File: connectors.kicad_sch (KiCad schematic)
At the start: 31 parts, among them J2 SM08B-SRSS-TB, U23 SDA, U26 SCL, U31 9V

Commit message: routing...
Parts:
- removed TP4: M1, TestPoint:TestPoint_Pad_D1.0mm, symbol Connector:TestPoint
- removed TP5: M2, TestPoint:TestPoint_Pad_D1.0mm, symbol Connector:TestPoint
- removed TP6: M3, TestPoint:TestPoint_Pad_D1.0mm, symbol Connector:TestPoint
- removed TP7: M4, TestPoint:TestPoint_Pad_D1.0mm, symbol Connector:TestPoint
- added TP10: 5V_USB, TestPoint:TestPoint_Pad_D1.0mm, symbol Connector:TestPoint
- added TP11: VCC_ICM, TestPoint:TestPoint_Pad_D1.0mm, symbol Connector:TestPoint
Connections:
- new net 5V_USB: TP10.1
- new net VCC_ICM: TP11.1

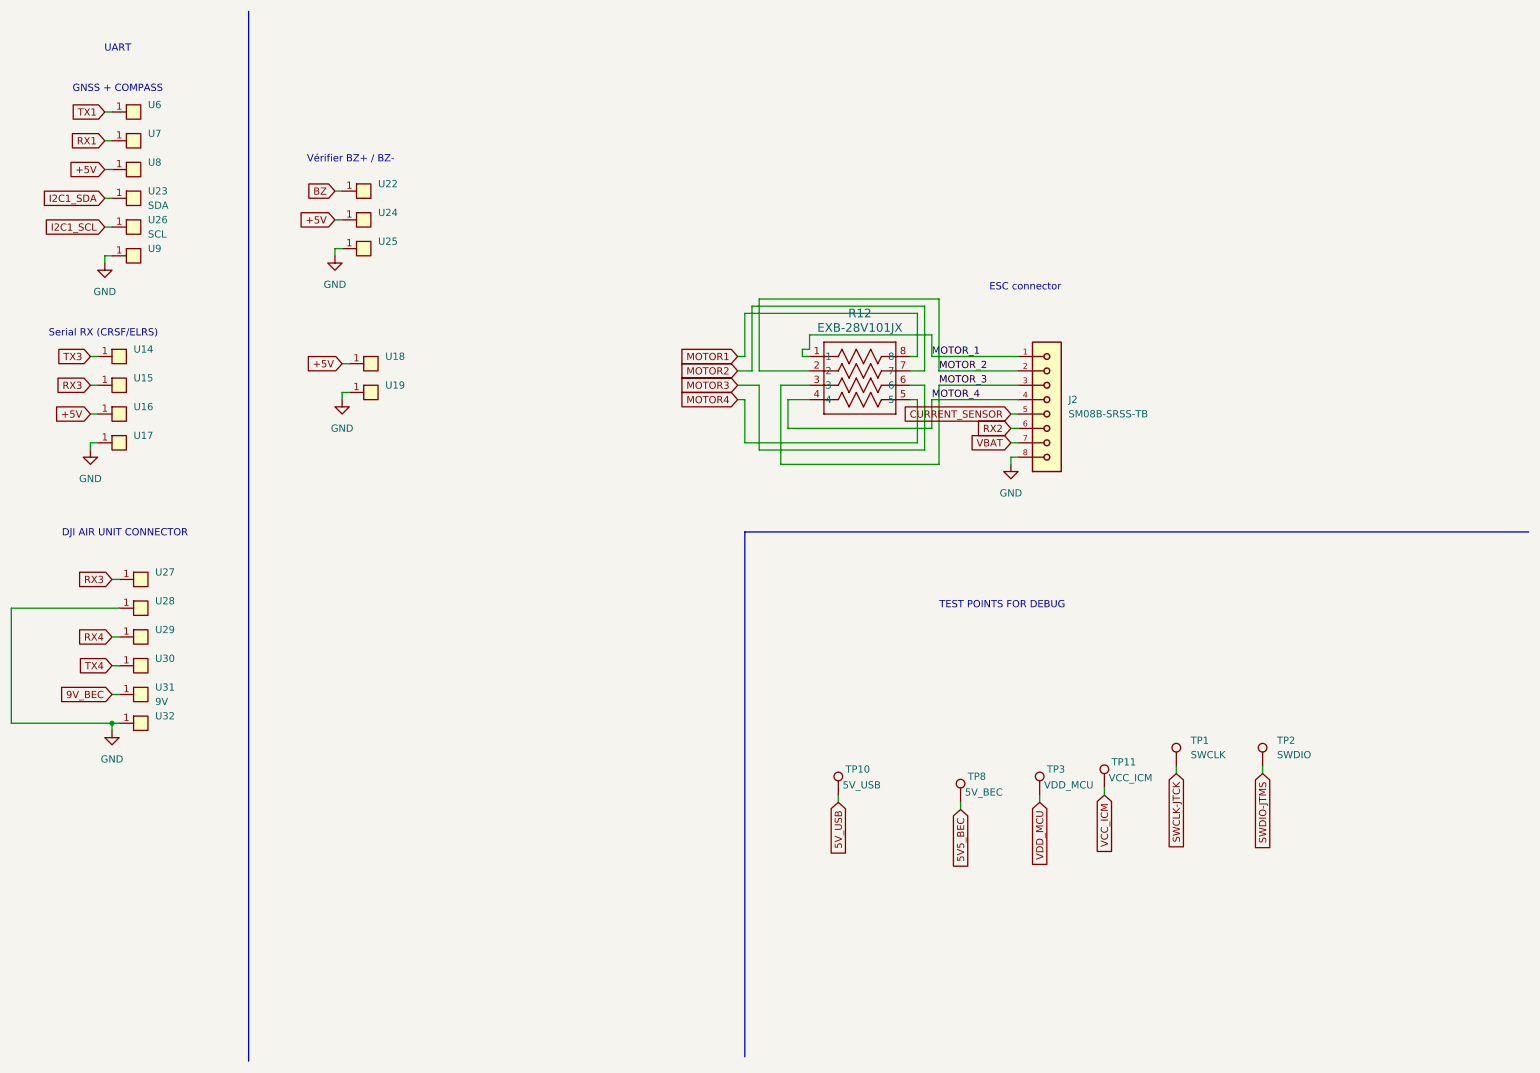
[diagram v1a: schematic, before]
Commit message: changed barometer to BMP580 and completed BOM
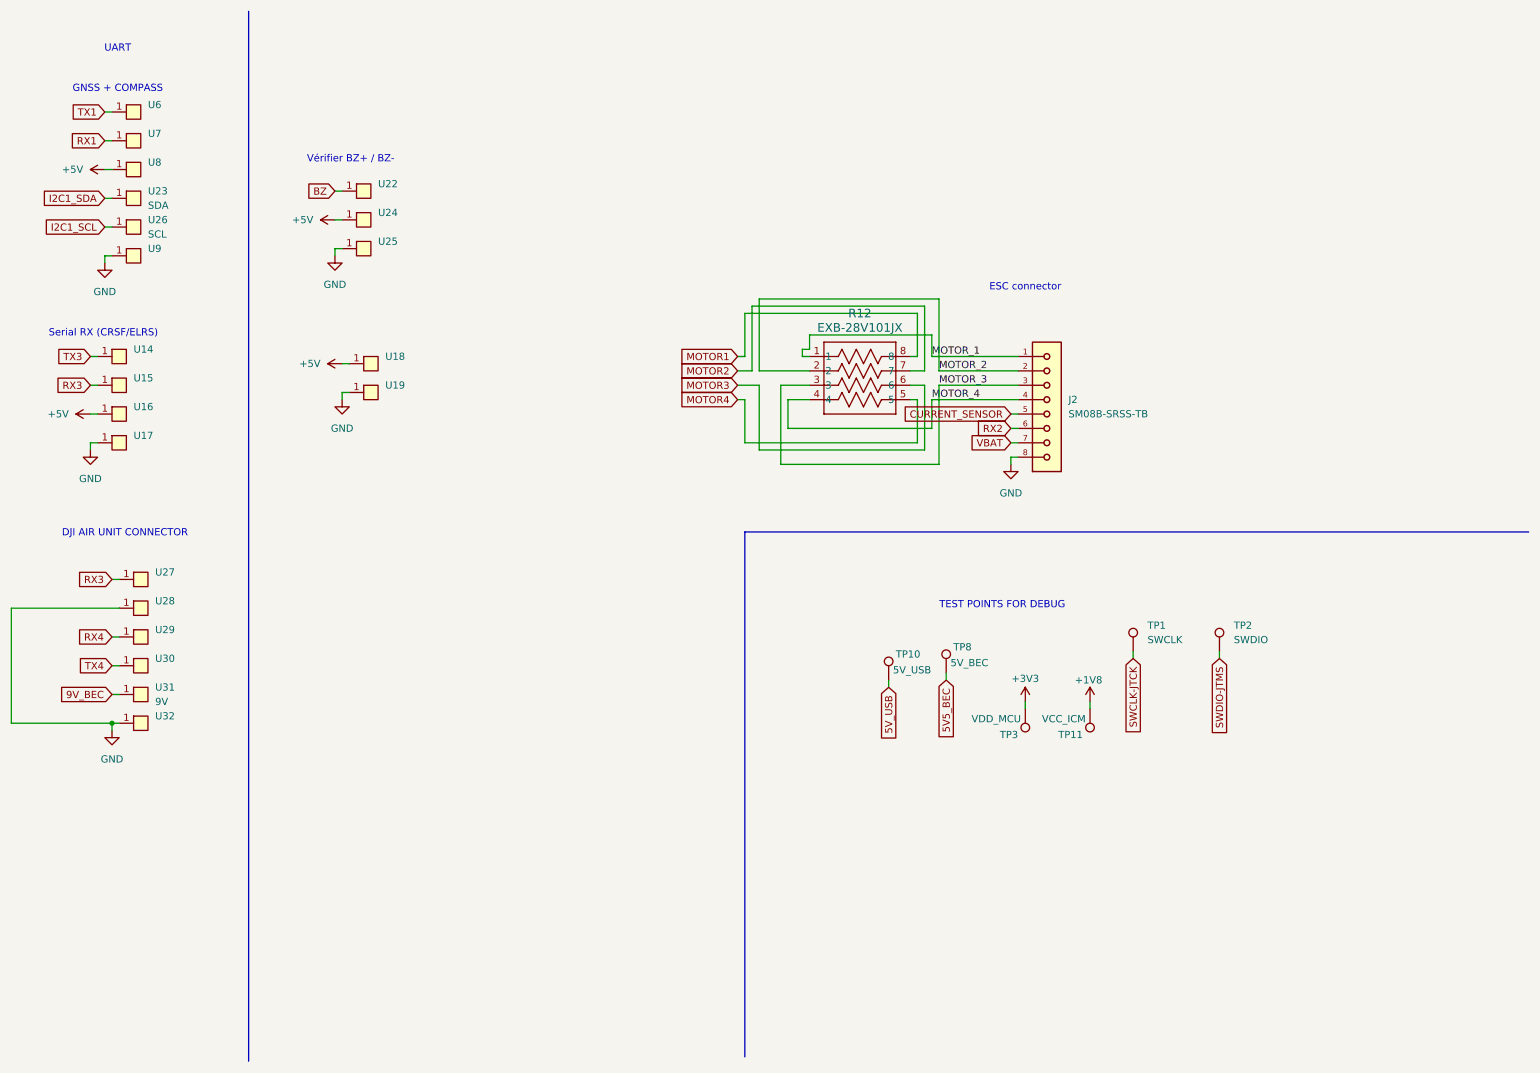
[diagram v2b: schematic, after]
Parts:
- R12: LCSC Part Name (none) -> C326873
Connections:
- net VCC_ICM renamed +1V8
- net VDD_MCU renamed +3V3
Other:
- moved on the sheet: TP1, TP10, TP11, TP2, TP3, TP8

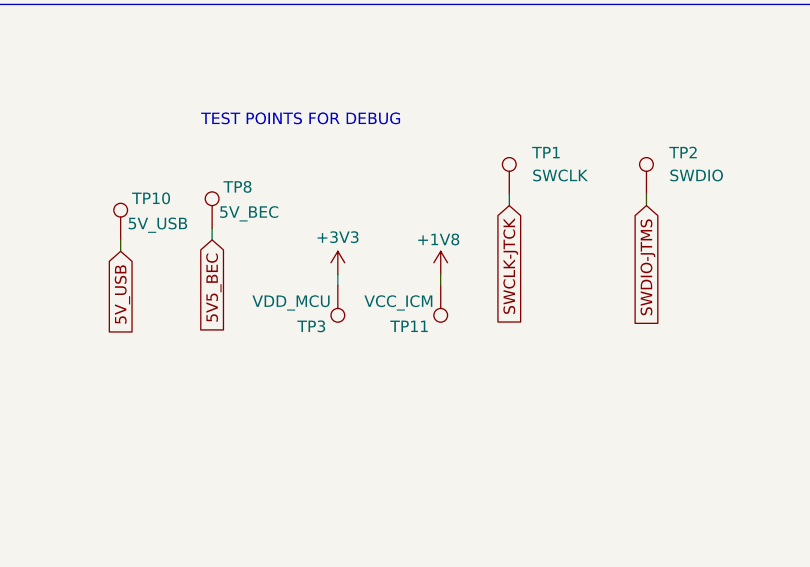
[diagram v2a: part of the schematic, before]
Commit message: switch IMU to BMI270
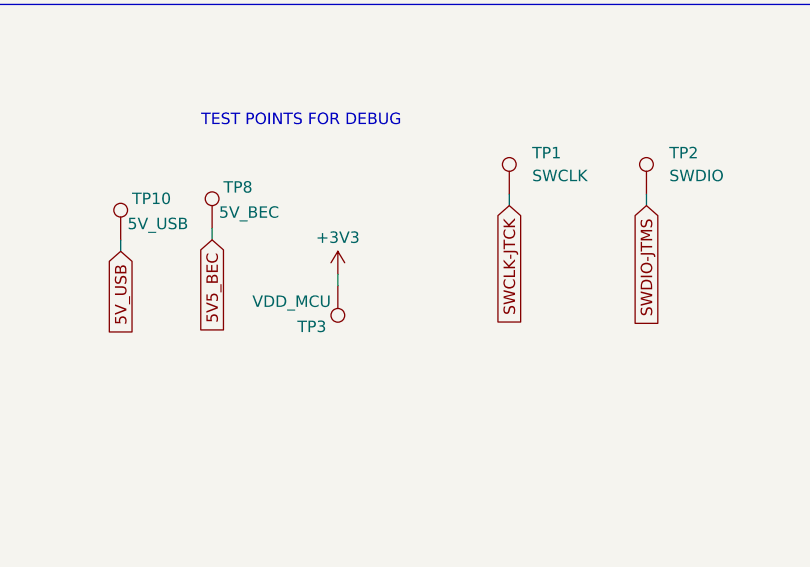
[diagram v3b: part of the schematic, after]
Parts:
- removed TP11: VCC_ICM, TestPoint:TestPoint_Pad_D1.0mm, symbol Connector:TestPoint
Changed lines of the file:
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@@
 	(wire
 		(pts
-			(xy 207.01 134.62) (xy 207.01 135.89)
-		)
-		(stroke
-			(width 0)
-			(type default)
-		)
-	)
-	(wire
-		(pts
 			(xy 73.66 49.53) (xy 74.93 49.53)
 		)
@@
 	(symbol
 		(lib_id "Connector:TestPoint")
-		(at 207.01 135.89 180)
-		(unit 1)
-		(exclude_from_sim no)
-		(in_bom no)
-		(on_board yes)
-		(dnp no)
-		(property "Reference" "TP11"
-			(at 205.74 140.462 0)
-			(effects
-				(font
-					(size 1.27 1.27)
-				)
-				(justify left)
-			)
-		)
-		(property "Value" "VCC_ICM"
-			(at 206.248 137.668 0)
-			(effects
-				(font
-					(size 1.27 1.27)
-				)
-				(justify left)
-			)
-		)
-		(property "Footprint" "TestPoint:TestPoint_Pad_D1.0mm"
-			(at 201.93 135.89 0)
-			(effects
-				(font
-					(size 1.27 1.27)
-				)
-				(hide yes)
-			)
-		)
-		(property "Datasheet" "~"
-			(at 201.93 135.89 0)
-			(effects
-				(font
-					(size 1.27 1.27)
-				)
-				(hide yes)
-			)
-		)
-		(property "Description" "test point"
-			(at 207.01 135.89 0)
-			(effects
-				(font
-					(size 1.27 1.27)
-				)
-				(hide yes)
-			)
-		)
-		(property "Availability" ""
-			(at 207.01 135.89 0)
-			(effects
-				(font
-					(size 1.27 1.27)
-				)
-				(hide yes)
-			)
-		)
-		(property "Price" ""
-			(at 207.01 135.89 0)
-			(effects
-				(font
-					(size 1.27 1.27)
-				)
-				(hide yes)
-			)
-		)
-		(pin "1"
-		)
-		(instances
-			(project "fcg4"
-				(path "/ebe93c2f-0aae-4f69-99fc-930f63b0ac94/895fabe0-ab4c-4c61-9719-dac54426ec22"
-					(reference "TP11")
-					(unit 1)
-				)
-			)
-		)
-	)
-	(symbol
-		(lib_id "Connector:TestPoint")
 		(at 214.63 125.73 0)
 		(unit 1)
@@
 					(unit 1)
 				)
-			)
-		)
-	)
-	(symbol
-		(lib_id "power:+1V8")
-		(at 207.01 134.62 0)
-		(unit 1)
-		(exclude_from_sim no)
-		(in_bom yes)
-		(on_board yes)
-		(dnp no)
-		(property "Reference" "#PWR022"
-			(at 207.01 138.43 0)
-			(effects
-				(font
-					(size 1.27 1.27)
-				)
-				(hide yes)
-			)
-		)
-		(property "Value" "+1V8"
-			(at 206.756 130.81 0)
-			(effects
-				(font
-					(size 1.27 1.27)
-				)
-			)
-		)
-		(property "Footprint" ""
-			(at 207.01 134.62 0)
-			(effects
-				(font
-					(size 1.27 1.27)
-				)
-				(hide yes)
-			)
-		)
-		(property "Datasheet" ""
-			(at 207.01 134.62 0)
-			(effects
-				(font
-					(size 1.27 1.27)
-				)
-				(hide yes)
-			)
-		)
-		(property "Description" "Power symbol creates a global label with name \"+1V8\""
-			(at 207.01 134.62 0)
-			(effects
-				(font
-					(size 1.27 1.27)
-				)
-				(hide yes)
-			)
-		)
-		(pin "1"
-		)
-		(instances
-			(project "fcg4"
-				(path "/ebe93c2f-0aae-4f69-99fc-930f63b0ac94/895fabe0-ab4c-4c61-9719-dac54426ec22"
-					(reference "#PWR022")
-					(unit 1)
-				)

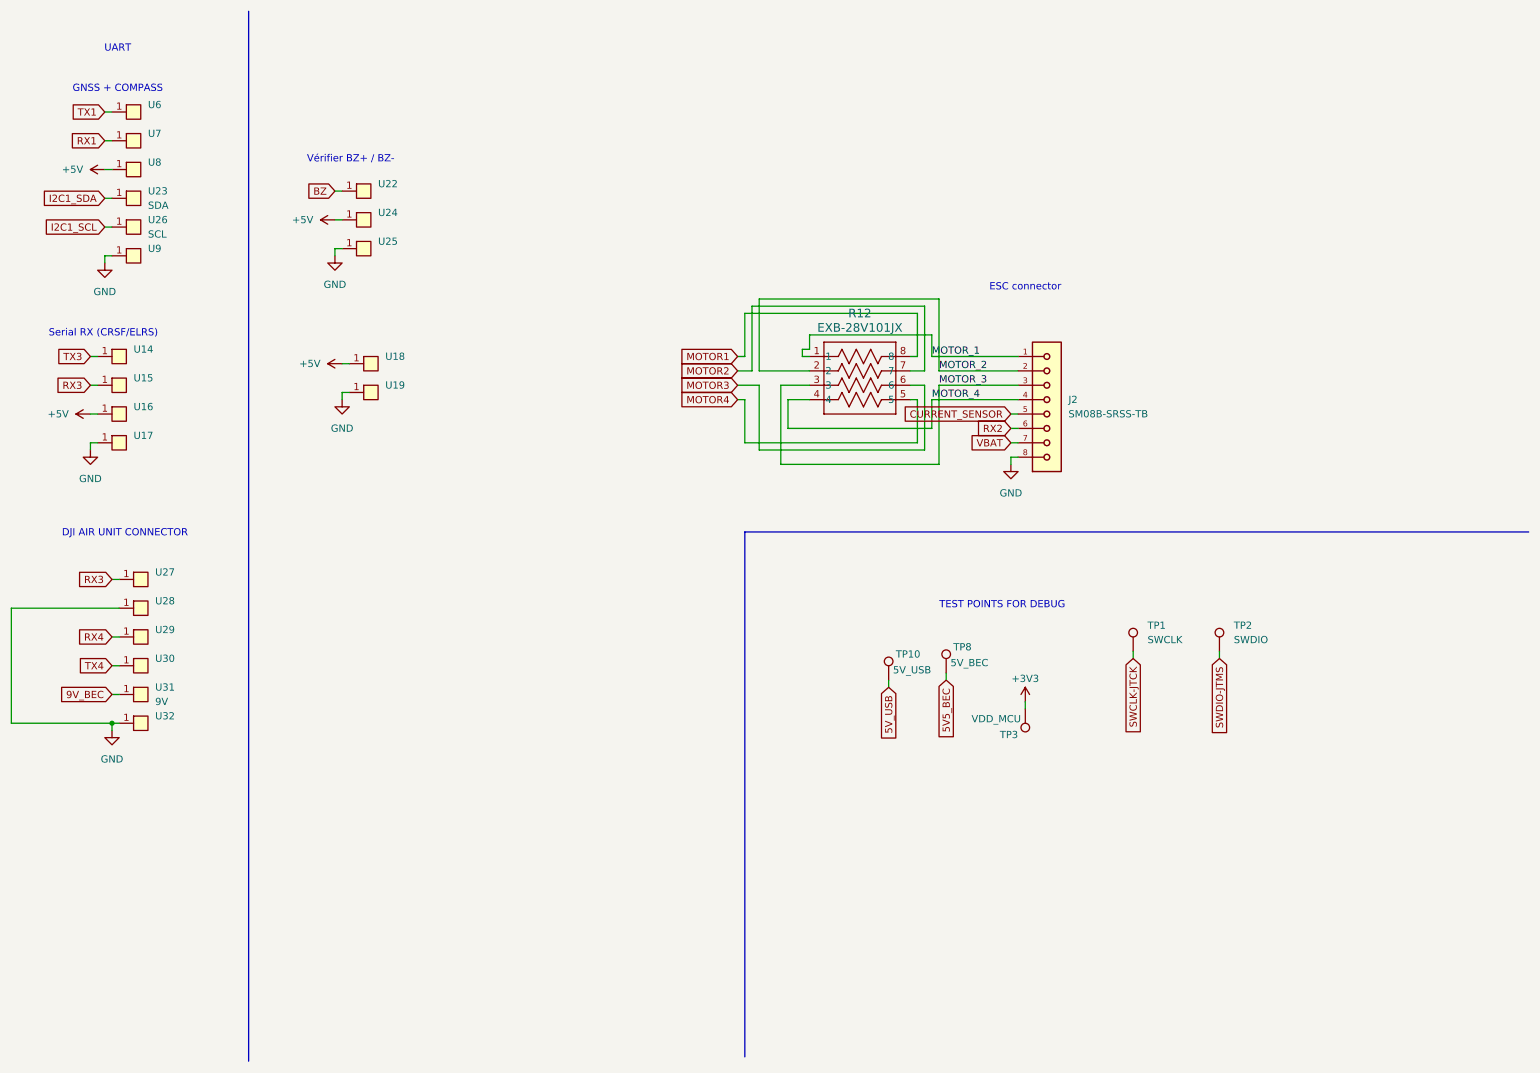
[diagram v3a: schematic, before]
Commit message: add microsd card connector
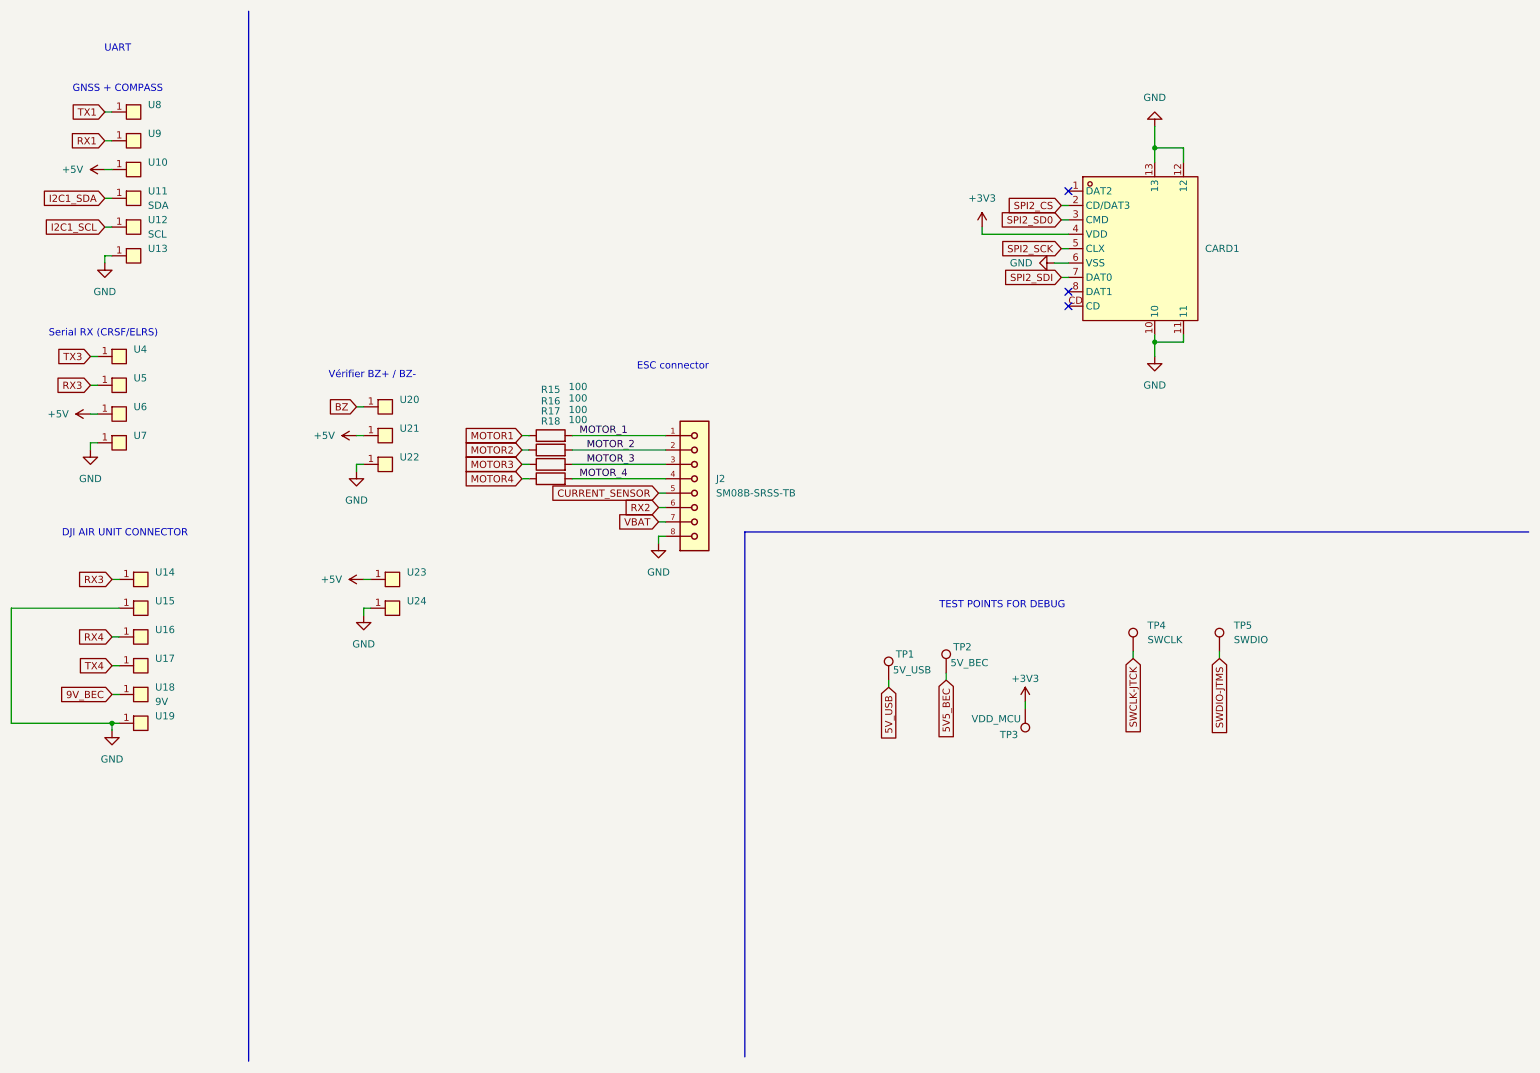
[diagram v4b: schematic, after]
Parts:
- removed R12: EXB-28V101JX, fcg4_fp:EXB28V_PAN, symbol fcg4:EXB-28V101JX
- added CARD1: (no value), fcg4_fp:TF-SMD_TF-PUSH, symbol fcg4:TF PUSH
- added R15, R16, R17, R18: 100, Resistor_SMD:R_0603_1608Metric, symbol Device:R
- U10: renamed from U8; value ~ -> (none)
- U13: renamed from U9; value ~ -> (none)
- U14: renamed from U27; value ~ -> (none)
- U15: renamed from U28; value ~ -> (none)
- U16: renamed from U29; value ~ -> (none)
- U17: renamed from U30; value ~ -> (none)
- U19: renamed from U32; value ~ -> (none)
- U20: renamed from U22; value ~ -> (none)
- U21: renamed from U24; value ~ -> (none)
- U22: renamed from U25; value ~ -> (none)
- U23: renamed from U18; value ~ -> (none)
- U24: renamed from U19; value ~ -> (none)
- U4: renamed from U14; value ~ -> (none)
- U5: renamed from U15; value ~ -> (none)
- U6: renamed from U16; value ~ -> (none)
- U7: renamed from U17; value ~ -> (none)
- U8: renamed from U6; value ~ -> (none)
- U9: renamed from U7; value ~ -> (none)
- renumbered TP10 to TP1, TP8 to TP2, TP1 to TP4, TP2 to TP5, U23 to U11, U26 to U12, U31 to U18
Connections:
- net +3V3: now also CARD1.4 (VDD)
- net GND: now also CARD1.10, CARD1.11, CARD1.12, CARD1.13, CARD1.6 (VSS)
- net MOTOR1: now also R15.1
- net MOTOR2: now also R16.1
- net MOTOR3: now also R17.1
- net MOTOR4: now also R18.1
- net MOTOR_1: now also R15.2
- net MOTOR_2: now also R16.2
- net MOTOR_3: now also R17.2
- net MOTOR_4: now also R18.2
- new net SPI2_CS: CARD1.2 (CD/DAT3)
- new net SPI2_SCK: CARD1.5 (CLX)
- new net SPI2_SD0: CARD1.3 (CMD)
- new net SPI2_SDI: CARD1.7 (DAT0)
- no-connect marks 0 -> 3
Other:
- moved on the sheet: J2, U20, U21, U22, U23, U24
